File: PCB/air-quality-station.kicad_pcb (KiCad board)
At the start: 2 copper layers, 13 parts, among them U1 ESP32-C6-MINI-1/U, U2 SCD41-D-R2, U3 BMP280, U4 TLV73333PDBV

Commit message: Add ESD component
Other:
- copper layers 2 -> 4
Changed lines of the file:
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@@
 	(paper "A4")
 	(layers
-		(0 "F.Cu" signal)
+		(0 "F.Cu" jumper)
+		(1 "In1.Cu" signal)
+		(2 "In2.Cu" signal)
 		(31 "B.Cu" signal)
 		(32 "B.Adhes" user "B.Adhesive")
@@
 	)
 	(setup
+		(stackup
+			(layer "F.SilkS"
+				(type "Top Silk Screen")
+			)
+			(layer "F.Paste"
+				(type "Top Solder Paste")
+			)
+			(layer "F.Mask"
+				(type "Top Solder Mask")
+				(thickness 0.01)
+			)
+			(layer "F.Cu"
+				(type "copper")
+				(thickness 0.035)
+			)
+			(layer "dielectric 1"
+				(type "prepreg")
+				(thickness 0.1)
+				(material "FR4")
+				(epsilon_r 4.5)
+				(loss_tangent 0.02)
+			)
+			(layer "In1.Cu"
+				(type "copper")
+				(thickness 0.035)
+			)
+			(layer "dielectric 2"
+				(type "core")
+				(thickness 1.24)
+				(material "FR4")
+				(epsilon_r 4.5)
+				(loss_tangent 0.02)
+			)
+			(layer "In2.Cu"
+				(type "copper")
+				(thickness 0.035)
+			)
+			(layer "dielectric 3"
+				(type "prepreg")
+				(thickness 0.1)
+				(material "FR4")
+				(epsilon_r 4.5)
+				(loss_tangent 0.02)
+			)
+			(layer "B.Cu"
+				(type "copper")
+				(thickness 0.035)
+			)
+			(layer "B.Mask"
+				(type "Bottom Solder Mask")
+				(thickness 0.01)
+			)
+			(layer "B.Paste"
+				(type "Bottom Solder Paste")
+			)
+			(layer "B.SilkS"
+				(type "Bottom Silk Screen")
+			)
+			(copper_finish "None")
+			(dielectric_constraints no)
+		)
 		(pad_to_mask_clearance 0)
 		(allow_soldermask_bridges_in_footprints no)
@@
 		(tags "capacitor")
 		(property "Reference" "C3"
-			(at 0.14 1.27 360)
+			(at 0.14 1.27 0)
 			(layer "F.SilkS")
 			(effects
@@
 		)
 		(property "Value" "100nF"
-			(at 0 1.43 360)
+			(at 0 1.43 0)
 			(layer "F.Fab")
 			(hide yes)
@@
 		)
 		(fp_text user "${REFERENCE}"
-			(at 0 0 360)
+			(at 0 0 0)
 			(layer "F.Fab")
 			(effects
@@
 		)
 	)
+	(gr_rect
+		(start 97.79 45.085)
+		(end 197.485 144.78)
+		(stroke
+			(width 0.2)
+			(type default)
+		)
+		(fill none)
+		(layer "In1.Cu")
+	)
 	(segment

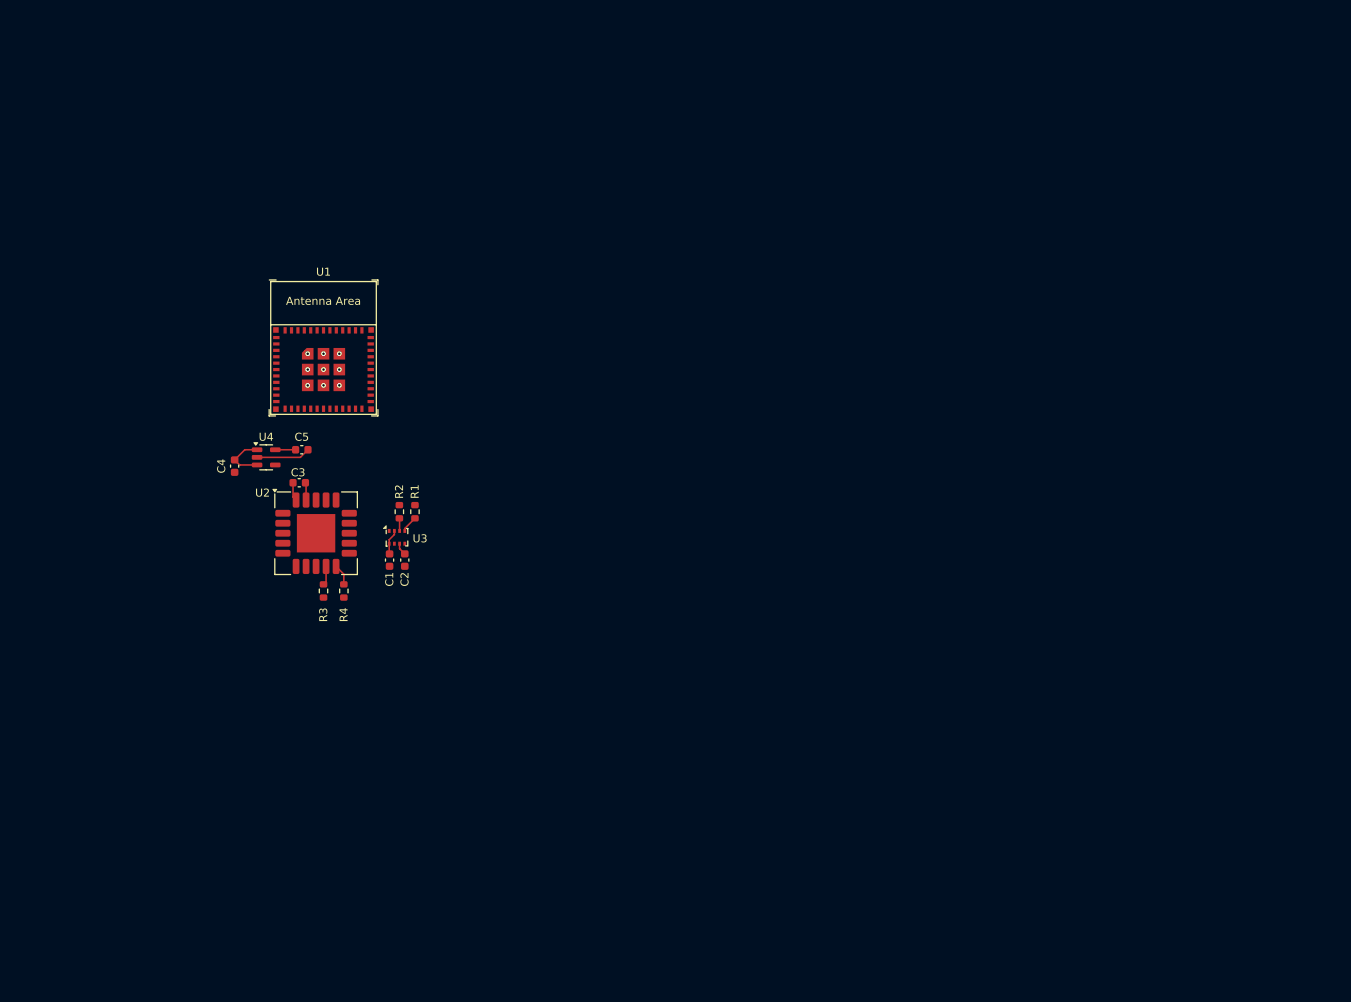
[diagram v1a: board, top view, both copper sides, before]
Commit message: Add E-Paper and Headers to schematic
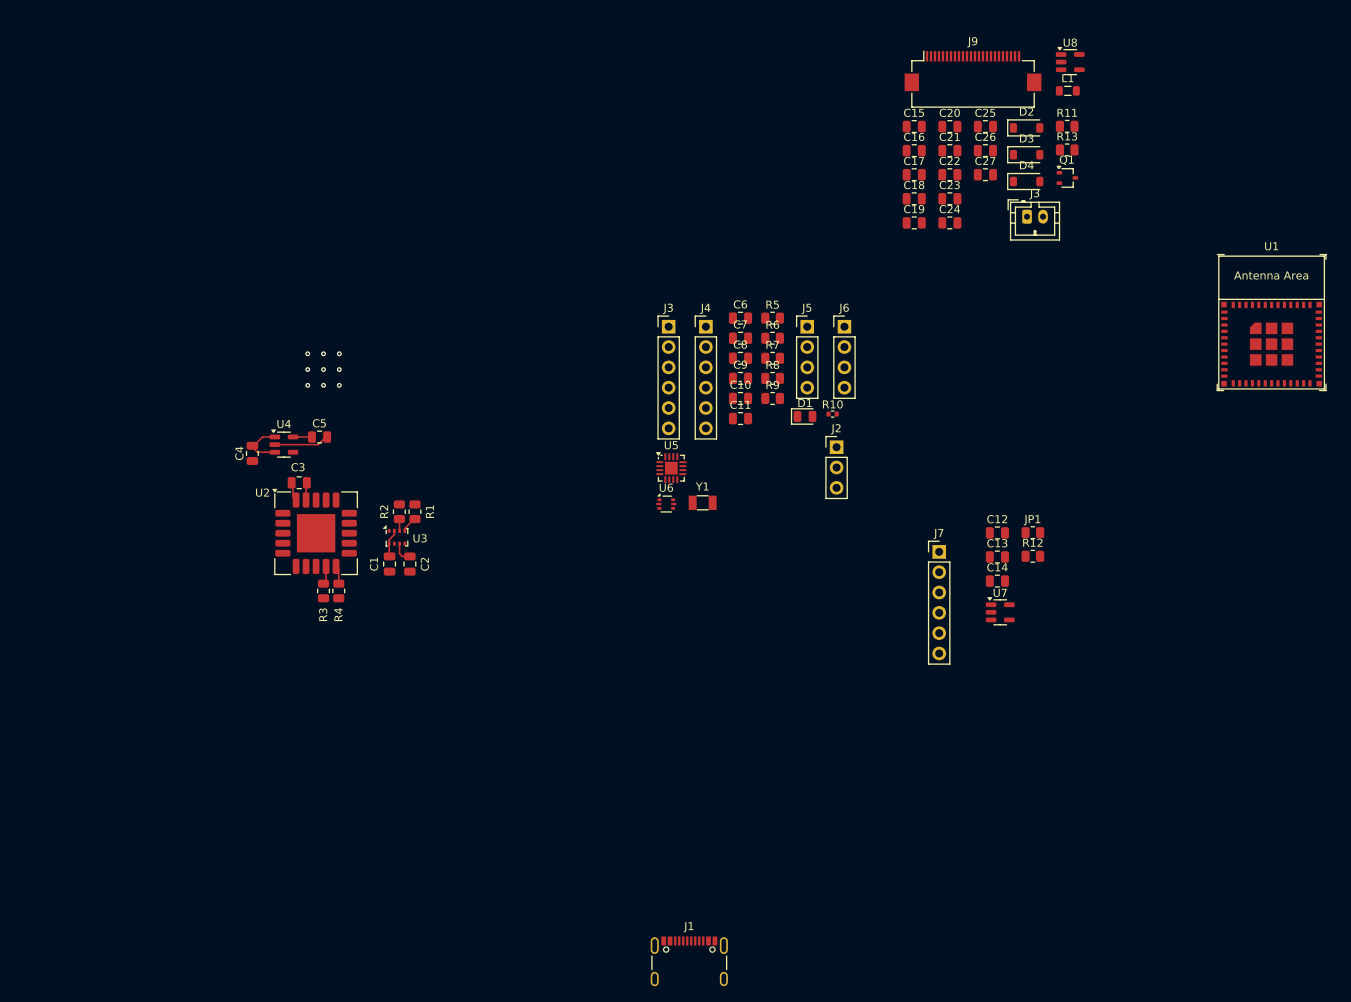
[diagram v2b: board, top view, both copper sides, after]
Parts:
- added C10: 12pF, Capacitor_SMD:C_0805_2012Metric, F.Cu at (118.2, 69.5)
- added C11: 12pF, Capacitor_SMD:C_0805_2012Metric, F.Cu at (118.2, 72.0)
- added C12: 100nF, Capacitor_SMD:C_0805_2012Metric, F.Cu at (150.3, 86.3)
- added C13: 100nF, Capacitor_SMD:C_0805_2012Metric, F.Cu at (150.3, 89.3)
- added C14: 4.7uF, Capacitor_SMD:C_0805_2012Metric, F.Cu at (150.3, 92.3)
- added C15: 1uF, Capacitor_SMD:C_0805_2012Metric, F.Cu at (139.9, 35.5)
- added C16: 1uF, Capacitor_SMD:C_0805_2012Metric, F.Cu at (139.9, 38.5)
- added C17: 1uF, Capacitor_SMD:C_0805_2012Metric, F.Cu at (139.9, 41.5)
- added C18: 1uF, Capacitor_SMD:C_0805_2012Metric, F.Cu at (139.9, 44.5)
- added C19: 1uF, Capacitor_SMD:C_0805_2012Metric, F.Cu at (139.9, 47.5)
- added C20: 1uF, Capacitor_SMD:C_0805_2012Metric, F.Cu at (144.3, 35.5)
- added C21: 4.7uF, Capacitor_SMD:C_0805_2012Metric, F.Cu at (144.3, 38.5)
- added C22: 4.7uF, Capacitor_SMD:C_0805_2012Metric, F.Cu at (144.3, 41.5)
- added C23: 1uF, Capacitor_SMD:C_0805_2012Metric, F.Cu at (144.3, 44.5)
- added C24: 4.7uF, Capacitor_SMD:C_0805_2012Metric, F.Cu at (144.3, 47.5)
- added C25: 100nF, Capacitor_SMD:C_0805_2012Metric, F.Cu at (148.8, 35.5)
- added C26: 100nF, Capacitor_SMD:C_0805_2012Metric, F.Cu at (148.8, 38.5)
- added C27: 1uF, Capacitor_SMD:C_0805_2012Metric, F.Cu at (148.8, 41.5)
- added C6: 1uF, Capacitor_SMD:C_0805_2012Metric, F.Cu at (118.2, 59.4)
- added C7: 4.7uF, Capacitor_SMD:C_0805_2012Metric, F.Cu at (118.2, 61.9)
- added C8: 100nF, Capacitor_SMD:C_0805_2012Metric, F.Cu at (118.2, 64.5)
- added C9: 1uF, Capacitor_SMD:C_0805_2012Metric, F.Cu at (118.2, 67.0)
- added D1: LED, LED_SMD:LED_0805_2012Metric, F.Cu at (126.2, 71.7)
- added D2: MBR0530, Diode_SMD:D_SOD-123, F.Cu at (153.9, 35.7)
- added D3: MBR0530, Diode_SMD:D_SOD-123, F.Cu at (153.9, 39.0)
- added D4: MBR0530, Diode_SMD:D_SOD-123, F.Cu at (153.9, 42.4)
- added J1: USB_C_Receptacle_USB2.0_16P, Connector_USB:USB_C_Receptacle_GCT_USB4105-xx-A_16P_TopMnt_Horizontal, F.Cu at (111.8, 141.0)
- added J2: Conn_01x03_Pin, Connector_PinHeader_2.54mm:PinHeader_1x03_P2.54mm_Vertical, F.Cu at (130.2, 75.6)
- added J3: Conn_01x06_Pin, Connector_PinHeader_2.54mm:PinHeader_1x06_P2.54mm_Vertical, F.Cu at (109.2, 60.5)
- added J3: JST_PH_BATTERY, Connector_JST:JST_PH_B2B-PH-K_1x02_P2.00mm_Vertical, F.Cu at (154.0, 46.8)
- added J4: SEN55, Connector_PinHeader_2.54mm:PinHeader_1x06_P2.54mm_Vertical, F.Cu at (113.8, 60.5)
- added J5: I2C_1, Connector_PinHeader_2.54mm:PinHeader_1x04_P2.54mm_Vertical, F.Cu at (126.5, 60.5)
- added J6: I2C_2, Connector_PinHeader_2.54mm:PinHeader_1x04_P2.54mm_Vertical, F.Cu at (131.2, 60.5)
- added J7: Conn_01x06_Pin, Connector_PinHeader_2.54mm:PinHeader_1x06_P2.54mm_Vertical, F.Cu at (143.0, 88.7)
- added J9: E-Paper, Connector_FFC-FPC:Hirose_FH12-24S-0.5SH_1x24-1MP_P0.50mm_Horizontal, F.Cu at (147.2, 28.6)
- added JP1: ~, Resistor_SMD:R_0805_2012Metric, F.Cu at (154.7, 86.2)
- added L1: 68uH, Inductor_SMD:L_0805_2012Metric, F.Cu at (159.1, 31.0)
- added Q1: Si1308EDL, Package_TO_SOT_SMD:SOT-323_SC-70, F.Cu at (159.0, 41.9)
- added R10: 10M, Resistor_SMD:R_0402_1005Metric, F.Cu at (129.7, 71.4)
- added R11: 10K, Resistor_SMD:R_0805_2012Metric, F.Cu at (159.0, 35.5)
- added R12: 2K, Resistor_SMD:R_0805_2012Metric, F.Cu at (154.7, 89.2)
- added R13: 0.47R, Resistor_SMD:R_0805_2012Metric, F.Cu at (159.0, 38.4)
- added R5: 5.1K, Resistor_SMD:R_0805_2012Metric, F.Cu at (122.2, 59.4)
- added R6: 5.1K, Resistor_SMD:R_0805_2012Metric, F.Cu at (122.2, 61.9)
- added R7: 10K, Resistor_SMD:R_0805_2012Metric, F.Cu at (122.2, 64.5)
- added R8: 10K, Resistor_SMD:R_0805_2012Metric, F.Cu at (122.2, 67.0)
- added R9: 10K, Resistor_SMD:R_0805_2012Metric, F.Cu at (122.2, 69.5)
- added U5: BQ24075RGT, Package_DFN_QFN:VQFN-16-1EP_3x3mm_P0.5mm_EP1.6x1.6mm, F.Cu at (109.5, 78.2)
- added U6: USBLC6-2P6, Package_TO_SOT_SMD:SOT-666, F.Cu at (108.9, 82.7)
- added U7: TLV73333PDBV, Package_TO_SOT_SMD:SOT-23-5, F.Cu at (150.6, 96.2)
- added U8: TLV73333PDBV, Package_TO_SOT_SMD:SOT-23-5, F.Cu at (159.4, 27.4)
- added Y1: 32.768kHz, Crystal:Crystal_SMD_3215-2Pin_3.2x1.5mm, F.Cu at (113.4, 82.5)
- C1, C2, C3, C4, C5: footprint Capacitor_SMD:C_0603_1608Metric -> Capacitor_SMD:C_0805_2012Metric
- R1, R2, R3, R4: footprint Resistor_SMD:R_0603_1608Metric -> Resistor_SMD:R_0805_2012Metric
- moved U1 118.6 mm to (184.6, 60.0)
- moved C4 2.73 mm to (57.1, 76.3)
- moved C5 2.73 mm to (65.5, 74.3)
- moved U4 2.73 mm to (61.1, 75.2)
- moved C2 0.81 mm to (76.8, 90.2)
- moved R4 0.64 mm to (67.9, 93.5)
- moved C1 0.50 mm to (74.3, 90.2)
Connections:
- C1 pad 1: GND -> SCL
- C1 pad 2: +3.3V -> SCL
- C2 pad 1: +3.3V -> SCL
- C2 pad 2: GND -> SCL
- C3 pad 1: +3.3V -> SCL
- C3 pad 2: GND -> SCL
- C4 pad 2: GND -> SCL
- C5 pad 1: +3V3 -> SCL
- C5 pad 2: GND -> SCL
- R1 pad 1: +3.3V -> SCL
- R2 pad 1: +3.3V -> SCL
- R2 pad 2: SDA -> SCL
- R3 pad 1: +3.3V -> SCL
- R4 pad 1: +3.3V -> SCL
- R4 pad 2: SDA -> SCL
- U1 pad 1: Net-(U1-GND-Pad1) -> SCL
- U1 pad 11: Net-(U1-GND-Pad1) -> SCL
- U1 pad 12: unconnected-(U1-GPIO0/ADC1_CH0/XTAL_32K_P-Pad12) -> Net-(U1-GPIO0/ADC1_CH0/XTAL_32K_P)
- U1 pad 13: unconnected-(U1-GPIO1/ADC1_CH1/XTAL_32K_N-Pad13) -> Net-(U1-GPIO1/ADC1_CH1/XTAL_32K_N)
- U1 pad 14: Net-(U1-GND-Pad1) -> SCL
- U1 pad 15: unconnected-(U1-MTCK/GPIO6/ADC1_CH6-Pad15) -> IO6_SCLK
- U1 pad 16: unconnected-(U1-MTDO/GPIO7-Pad16) -> IO7_SDI
- U1 pad 17: unconnected-(U1-GPIO12/USB_D--Pad17) -> D-
- U1 pad 18: unconnected-(U1-GPIO13/USB_D+-Pad18) -> D+
- U1 pad 19: unconnected-(U1-GPIO14-Pad19) -> IO14_RES
- U1 pad 2: Net-(U1-GND-Pad1) -> SCL
- U1 pad 20: unconnected-(U1-GPIO15-Pad20) -> IO15_DC
- U1 pad 24: unconnected-(U1-GPIO18-Pad24) -> IO18_CS
- U1 pad 26: SDA -> SCL
- U1 pad 3: unconnected-(U1-3V3-Pad3) -> +3V3_MCU
- U1 pad 30: unconnected-(U1-U0RXD/GPIO17-Pad30) -> UART_RX
- U1 pad 31: unconnected-(U1-U0TXD/GPIO16-Pad31) -> UART_TX
- U1 pad 36: Net-(U1-GND-Pad1) -> SCL
- U1 pad 37: Net-(U1-GND-Pad1) -> SCL
- U1 pad 38: Net-(U1-GND-Pad1) -> SCL
- U1 pad 39: Net-(U1-GND-Pad1) -> SCL
- U1 pad 40: Net-(U1-GND-Pad1) -> SCL
- U1 pad 41: Net-(U1-GND-Pad1) -> SCL
- U1 pad 42: Net-(U1-GND-Pad1) -> SCL
- U1 pad 43: Net-(U1-GND-Pad1) -> SCL
- U1 pad 44: Net-(U1-GND-Pad1) -> SCL
- U1 pad 45: Net-(U1-GND-Pad1) -> SCL
- U1 pad 46: Net-(U1-GND-Pad1) -> SCL
- U1 pad 47: Net-(U1-GND-Pad1) -> SCL
- U1 pad 48: Net-(U1-GND-Pad1) -> SCL
- U1 pad 49: Net-(U1-GND-Pad1) -> SCL
- U1 pad 50: Net-(U1-GND-Pad1) -> SCL
- U1 pad 51: Net-(U1-GND-Pad1) -> SCL
- U1 pad 52: Net-(U1-GND-Pad1) -> SCL
- U1 pad 53: Net-(U1-GND-Pad1) -> SCL
- U1 pad 8: unconnected-(U1-EN/CHIP_PU-Pad8) -> VCC
- U1 pad 9: unconnected-(U1-MTMS/GPIO4/ADC1_CH4-Pad9) -> IO4_BUSY
- U2 pad 10: SDA -> SCL
- U2 pad 19: +3.3V -> SCL
- U2 pad 20: GND -> SCL
- U2 pad 21: GND -> SCL
- U2 pad 6: GND -> SCL
- U2 pad 7: +3.3V -> SCL
- U3 pad 1: GND -> SCL
- U3 pad 2: +3.3V -> SCL
- U3 pad 3: SDA -> SCL
- U3 pad 5: GND -> SCL
- U3 pad 6: +3.3V -> SCL
- U3 pad 7: GND -> SCL
- U3 pad 8: +3.3V -> SCL
- U4 pad 2: GND -> SCL
- U4 pad 5: +3V3 -> SCL
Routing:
- net SCL: track 4.47 -> 28.0 mm, vias 0 -> 9
- net GND: track 9.08 -> 0.00 mm
- net +3.3V: track 6.87 -> 0.00 mm
- net SDA: track 4.23 -> 0.00 mm
- net +3V3: track 2.54 -> 0.00 mm
- net Net-(U1-GND-Pad1): vias 9 -> 0

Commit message: ERC check and fixes
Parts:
- removed the J3 at (109.2, 60.5)
- removed the J3 at (154.0, 46.8)
- removed J7: Conn_01x06_Pin, Connector_PinHeader_2.54mm:PinHeader_1x06_P2.54mm_Vertical
- added J3: JST_PH_BATTERY, Connector_JST:JST_PH_B2B-PH-K_1x02_P2.00mm_Vertical, F.Cu at (67.2, 37.9)
- J2: value Conn_01x03_Pin -> UART
- moved U1 133.2 mm to (52.3, 44.3)
- moved C12 125.4 mm to (33.8, 39.8)
- moved C13 125.4 mm to (33.8, 42.8)
- moved C14 125.4 mm to (33.8, 45.8)
- moved D2 115.0 mm to (41.7, 60.9)
- moved D4 115.0 mm to (41.7, 67.6)
- moved D3 115.0 mm to (41.7, 64.3)
- moved JP1 112.1 mm to (47.1, 54.8)
- moved J1 109.8 mm to (32.9, 64.5)
- moved C20 106.4 mm to (38.2, 42.8)
- moved C21 106.4 mm to (38.2, 45.8)
- moved C25 106.1 mm to (42.7, 36.8)
- moved C26 106.1 mm to (42.7, 39.8)
- moved C27 106.1 mm to (42.7, 42.8)
- moved U8 105.6 mm to (60.7, 65.0)
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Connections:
- C1 pad 1: SCL -> GND
- C1 pad 2: SCL -> +3V3_SEN
- C10 pad 2: SCL -> GND
- C11 pad 2: SCL -> GND
- C12 pad 2: SCL -> GND
- C13 pad 2: SCL -> GND
- C14 pad 1: SCL -> GND
- C15 pad 2: SCL -> GND
- C16 pad 2: SCL -> GND
- C17 pad 2: SCL -> GND
- C18 pad 2: SCL -> GND
- C19 pad 2: SCL -> GND
- C2 pad 1: SCL -> +3V3_SEN
- C2 pad 2: SCL -> GND
- C20 pad 2: SCL -> GND
- C22 pad 2: SCL -> GND
- C23 pad 2: SCL -> GND
- C24 pad 2: SCL -> GND
- C25 pad 2: SCL -> GND
- C26 pad 2: SCL -> GND
- C27 pad 2: SCL -> GND
- C3 pad 1: SCL -> +3V3_SEN
- C3 pad 2: SCL -> GND
- C4 pad 2: SCL -> GND
- C5 pad 1: SCL -> +3V3_SEN
- C5 pad 2: SCL -> GND
- C6 pad 2: SCL -> GND
- C7 pad 1: SCL -> GND
- C8 pad 2: SCL -> GND
- C9 pad 2: SCL -> GND
- D3 pad 1: SCL -> GND
- J1 pad A1: SCL -> GND
- J1 pad A12: SCL -> GND
- J1 pad B1: SCL -> GND
- J1 pad B12: SCL -> GND
- J1 pad S1: SCL -> GND
- J2 pad 1: SCL -> GND
- J4 pad 2: SCL -> GND
- J4 pad 3: SCL -> SDA
- J4 pad 5: SCL -> GND
- J5 pad 1: SCL -> GND
- J5 pad 2: SCL -> +3V3_SEN
- J5 pad 4: SCL -> SDA
- J6 pad 1: SCL -> GND
- J6 pad 2: SCL -> +3V3_SEN
- J6 pad 4: SCL -> SDA
- J9 pad 17: SCL -> GND
- J9 pad 8: SCL -> GND
- R1 pad 1: SCL -> +3V3_SEN
- R11 pad 2: SCL -> GND
- R12 pad 1: SCL -> GND
- R13 pad 2: SCL -> GND
- R2 pad 1: SCL -> +3V3_SEN
- R2 pad 2: SCL -> SDA
- R3 pad 1: SCL -> +3V3_SEN
- R4 pad 1: SCL -> +3V3_SEN
- R4 pad 2: SCL -> SDA
- R5 pad 2: SCL -> GND
- R6 pad 2: SCL -> GND
- R7 pad 2: SCL -> GND
- R9 pad 2: SCL -> GND
- U1 pad 1: SCL -> GND
- U1 pad 11: SCL -> GND
- U1 pad 14: SCL -> GND
- U1 pad 2: SCL -> GND
- U1 pad 26: SCL -> SDA
- U1 pad 36: SCL -> GND
- U1 pad 37: SCL -> GND
- U1 pad 38: SCL -> GND
- U1 pad 39: SCL -> GND
- U1 pad 40: SCL -> GND
- U1 pad 41: SCL -> GND
- U1 pad 42: SCL -> GND
- U1 pad 43: SCL -> GND
- U1 pad 44: SCL -> GND
- U1 pad 45: SCL -> GND
- U1 pad 46: SCL -> GND
- U1 pad 47: SCL -> GND
- U1 pad 48: SCL -> GND
- U1 pad 49: SCL -> GND
- U1 pad 50: SCL -> GND
- U1 pad 51: SCL -> GND
- U1 pad 52: SCL -> GND
- U1 pad 53: SCL -> GND
- U1 pad 8: VCC -> +3V3_MCU
- U2 pad 10: SCL -> SDA
- U2 pad 19: SCL -> +3V3_SEN
- U2 pad 20: SCL -> GND
- U2 pad 21: SCL -> GND
- U2 pad 6: SCL -> GND
- U2 pad 7: SCL -> +3V3_SEN
- U3 pad 1: SCL -> GND
- U3 pad 2: SCL -> +3V3_SEN
- U3 pad 3: SCL -> SDA
- U3 pad 5: SCL -> GND
- U3 pad 6: SCL -> +3V3_SEN
- U3 pad 7: SCL -> GND
- U3 pad 8: SCL -> +3V3_SEN
- U4 pad 2: SCL -> GND
- U4 pad 5: SCL -> +3V3_SEN
- U5 pad 15: SCL -> GND
- U5 pad 17: SCL -> GND
- U5 pad 4: SCL -> GND
- U5 pad 5: SCL -> GND
- U5 pad 6: VDDH -> +5V
- U5 pad 8: SCL -> GND
- U6 pad 2: SCL -> GND
- U7 pad 2: SCL -> GND
- U8 pad 2: SCL -> GND
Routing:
- net SCL: track 28.0 -> 0.00 mm, vias 9 -> 0
- net +5V: track 6.40 -> 0.00 mm
